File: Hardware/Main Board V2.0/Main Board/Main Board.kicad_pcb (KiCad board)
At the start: 2 copper layers, 61 parts, among them J1 Module A1, J2 Module A2, J3 Module A3, J4 Module B1, J5 Module B2, J6 Module B3, U1 74AHCT595, U2 74AHCT595, U3 74AHCT595, U4 74AHCT595, U5 ESP32-WROOM-32UE-H4, U6 ESP32-WROOM-32UE-H4, U7 CP2104, U8 CP2104, U9 GT-USB-7051A

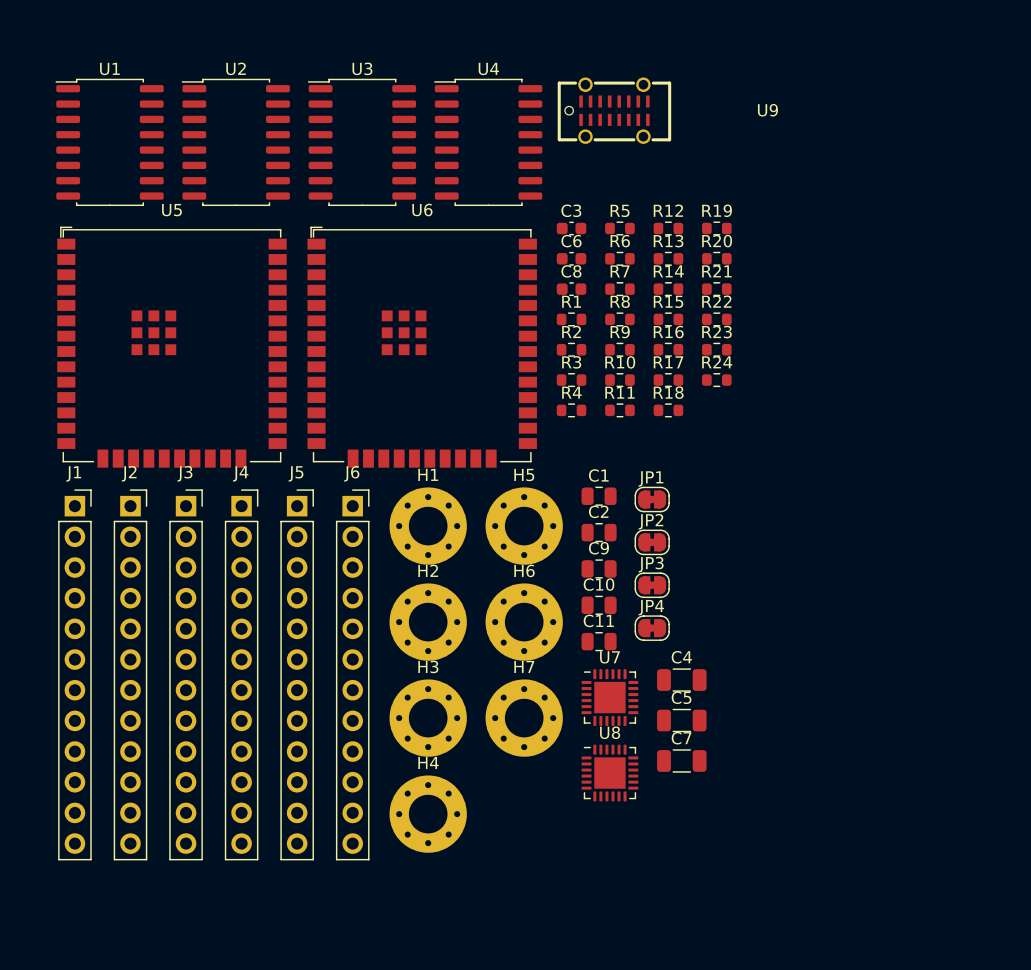
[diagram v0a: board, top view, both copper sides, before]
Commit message: Work on shift registers, and power for esp32
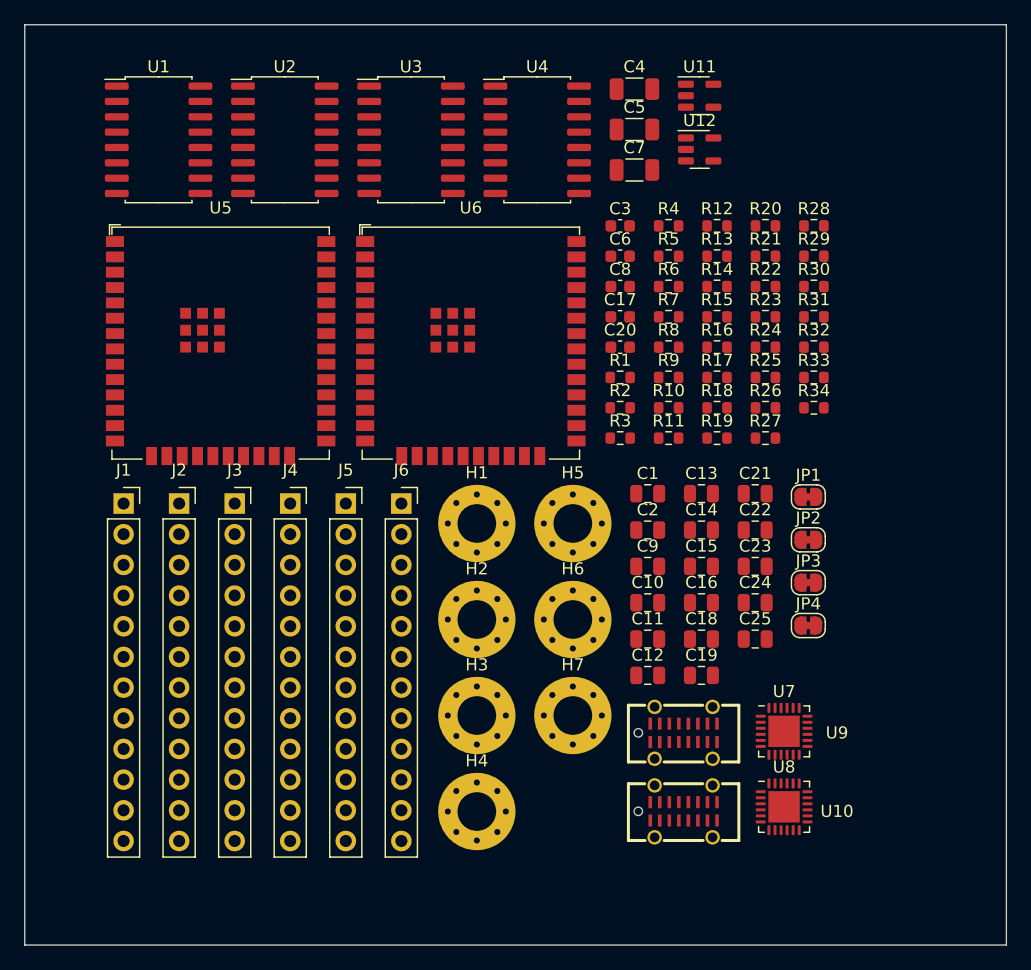
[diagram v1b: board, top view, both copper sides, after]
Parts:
- added C12: 1uF, Capacitor_SMD:C_0805_2012Metric, F.Cu at (71.9, 69.1)
- added C13: 1uF, Capacitor_SMD:C_0805_2012Metric, F.Cu at (76.4, 54.1)
- added C14: 10uF, Capacitor_SMD:C_0805_2012Metric, F.Cu at (76.4, 57.1)
- added C15: 4.7uF, Capacitor_SMD:C_0805_2012Metric, F.Cu at (76.4, 60.1)
- added C16: 1uF, Capacitor_SMD:C_0805_2012Metric, F.Cu at (76.4, 63.1)
- added C17: 100nF, Capacitor_SMD:C_0603_1608Metric, F.Cu at (69.6, 39.4)
- added C18: 4.7uF, Capacitor_SMD:C_0805_2012Metric, F.Cu at (76.4, 66.1)
- added C19: 1uF, Capacitor_SMD:C_0805_2012Metric, F.Cu at (76.4, 69.1)
- added C20: 100nF, Capacitor_SMD:C_0603_1608Metric, F.Cu at (69.6, 41.9)
- added C21: 10uF, Capacitor_SMD:C_0805_2012Metric, F.Cu at (80.8, 54.1)
- added C22: 1uF, Capacitor_SMD:C_0805_2012Metric, F.Cu at (80.8, 57.1)
- added C23: 10uF, Capacitor_SMD:C_0805_2012Metric, F.Cu at (80.8, 60.1)
- added C24: 10uF, Capacitor_SMD:C_0805_2012Metric, F.Cu at (80.8, 63.1)
- added C25: 1uF, Capacitor_SMD:C_0805_2012Metric, F.Cu at (80.8, 66.1)
- added R25: 5.1K, Resistor_SMD:R_0603_1608Metric, F.Cu at (81.7, 44.4)
- added R26: 5.1K, Resistor_SMD:R_0603_1608Metric, F.Cu at (81.7, 47.0)
- added R27: 5.1K, Resistor_SMD:R_0603_1608Metric, F.Cu at (81.7, 49.5)
- added R28: 5.1K, Resistor_SMD:R_0603_1608Metric, F.Cu at (85.7, 31.9)
- added R29: 10K, Resistor_SMD:R_0603_1608Metric, F.Cu at (85.7, 34.4)
- added R30: 10K, Resistor_SMD:R_0603_1608Metric, F.Cu at (85.7, 36.9)
- added R31: 100K, Resistor_SMD:R_0603_1608Metric, F.Cu at (85.7, 39.4)
- added R32: 4.3K, Resistor_SMD:R_0603_1608Metric, F.Cu at (85.7, 41.9)
- added R33: 100K, Resistor_SMD:R_0603_1608Metric, F.Cu at (85.7, 44.4)
- added R34: 4.3K, Resistor_SMD:R_0603_1608Metric, F.Cu at (85.7, 47.0)
- added U10: GT-USB-7051A, KiCad:GT-USB-7051A, F.Cu at (74.9, 80.4)
- added U11: AP2112K-3.3, Package_TO_SOT_SMD:SOT-23-5, F.Cu at (76.2, 21.1)
- added U12: AP2112K-3.3, Package_TO_SOT_SMD:SOT-23-5, F.Cu at (76.2, 25.6)
- moved U9 51.8 mm to (74.9, 73.9)
- moved C4 49.1 mm to (70.8, 20.6)
- moved C7 49.1 mm to (70.8, 27.3)
- moved C5 49.1 mm to (70.8, 23.9)
- moved R19 17.4 mm to (77.6, 49.5)
- moved R4 17.3 mm to (73.6, 31.9)
- moved U7 14.7 mm to (83.2, 73.7)
- moved U8 14.7 mm to (83.2, 80.0)
- moved JP1 12.9 mm to (85.2, 54.3)
- moved JP2 12.9 mm to (85.2, 57.9)
- moved JP3 12.9 mm to (85.2, 61.4)
- moved JP4 12.9 mm to (85.2, 65.0)
- moved R3 6.27 mm to (69.6, 49.5)
- moved R1 6.27 mm to (69.6, 44.4)
- moved R2 6.27 mm to (69.6, 47.0)
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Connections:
- C10 pad 1: unconnected-(C10-Pad1) -> Net-(U7-VPP)
- C10 pad 2: unconnected-(C10-Pad2) -> GND
- C11 pad 1: unconnected-(C11-Pad1) -> GND
- C11 pad 2: unconnected-(C11-Pad2) -> Net-(U8-VPP)
- C5 pad 1: +3V3 -> A_VCC
- C6 pad 1: +3V3 -> A_VCC
- C7 pad 1: +3V3 -> B_VCC
- C8 pad 1: +3V3 -> B_VCC
- J1 pad 3: VCC -> A_VCC
- J2 pad 3: VCC -> A_VCC
- J3 pad 3: VCC -> A_VCC
- J4 pad 3: VCC -> B_VCC
- J5 pad 3: VCC -> B_VCC
- J6 pad 3: VCC -> B_VCC
- R23 pad 2: +3V3 -> A_VCC
- R24 pad 2: +3V3 -> B_VCC
- U5 pad 2: +3V3 -> B_VCC
- U6 pad 2: +3V3 -> A_VCC
- U7 pad 16: unconnected-(U7-VPP-Pad16) -> Net-(U7-VPP)
- U7 pad 3: Net-(D19-L3) -> A_D+
- U7 pad 4: Net-(D19-L2) -> A_D-
- U7 pad 5: +3V3 -> A_VCC
- U7 pad 6: +3V3 -> A_VCC
- U7 pad 7: +3V3 -> A_VCC
- U8 pad 16: unconnected-(U8-VPP-Pad16) -> Net-(U8-VPP)
- U8 pad 3: Net-(D20-L3) -> B_D+
- U8 pad 4: Net-(D20-L2) -> B_D-
- U8 pad 5: +3V3 -> B_VCC
- U8 pad 6: +3V3 -> B_VCC
- U8 pad 7: +3V3 -> B_VCC
- U9 pad A1: unconnected-(U9-GND-PadA1) -> GND
- U9 pad A12: unconnected-(U9-GND-PadA12) -> GND
- U9 pad A4: unconnected-(U9-VBUS-PadA4) -> Net-(D22-A)
- U9 pad A5: unconnected-(U9-CC1-PadA5) -> B_CC1
- U9 pad A6: unconnected-(U9-DP1-PadA6) -> B_D+
- U9 pad A7: unconnected-(U9-DN1-PadA7) -> B_D-
- U9 pad A9: unconnected-(U9-VBUS-PadA9) -> Net-(D22-A)
- U9 pad B1: unconnected-(U9-GND-PadB1) -> GND
- U9 pad B12: unconnected-(U9-GND-PadB12) -> GND
- U9 pad B4: unconnected-(U9-VBUS-PadB4) -> Net-(D22-A)
- U9 pad B5: unconnected-(U9-CC2-PadB5) -> B_CC2
- U9 pad B6: unconnected-(U9-DP2-PadB6) -> B_D+
- U9 pad B7: unconnected-(U9-DN2-PadB7) -> B_D-
- U9 pad B9: unconnected-(U9-VBUS-PadB9) -> Net-(D22-A)
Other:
- board outline added: 81.3 x 76.2 mm

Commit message: v2 work
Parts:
- removed C22, C25: 1uF, Capacitor_SMD:C_0805_2012Metric
- removed C24: 10uF, Capacitor_SMD:C_0805_2012Metric
- removed J2: Module A2, Connector_PinSocket_2.54mm:PinSocket_1x12_P2.54mm_Vertical
- removed J3: Module A3, Connector_PinSocket_2.54mm:PinSocket_1x12_P2.54mm_Vertical
- removed J4: Module B1, Connector_PinSocket_2.54mm:PinSocket_1x12_P2.54mm_Vertical
- removed J6: Module B3, Connector_PinSocket_2.54mm:PinSocket_1x12_P2.54mm_Vertical
- added C26: 100nF, Capacitor_SMD:C_0603_1608Metric, F.Cu at (84.1, 121.3)
- added C27: 1uF, Capacitor_SMD:C_0805_2012Metric, F.Cu at (30.0, 178.4)
- added C28: 22uF, Capacitor_SMD:C_1206_3216Metric, F.Cu at (117.0, 119.0)
- added C29: 100nF, Capacitor_SMD:C_0603_1608Metric, F.Cu at (84.1, 123.8)
- added C30: 4.7uF, Capacitor_SMD:C_0805_2012Metric, F.Cu at (30.0, 181.4)
- added C31: 1uF, Capacitor_SMD:C_0805_2012Metric, F.Cu at (34.5, 169.4)
- added C32: 100nF, Capacitor_SMD:C_0603_1608Metric, F.Cu at (84.1, 126.3)
- added C33: 4.7uF, Capacitor_SMD:C_0805_2012Metric, F.Cu at (34.5, 172.4)
- added C34: 22uF, Capacitor_SMD:C_1206_3216Metric, F.Cu at (117.0, 122.3)
- added C35: 10uF, Capacitor_SMD:C_0805_2012Metric, F.Cu at (34.5, 175.4)
- added C36: 4.7uF, Capacitor_SMD:C_0805_2012Metric, F.Cu at (34.5, 178.4)
- added C37: 1uF, Capacitor_SMD:C_0805_2012Metric, F.Cu at (34.5, 181.4)
- added C38: 100nF, Capacitor_SMD:C_0603_1608Metric, F.Cu at (84.1, 128.8)
- added C39: 10nF, Capacitor_SMD:C_0603_1608Metric, F.Cu at (84.1, 131.3)
- added D1: Emerald, LED_SMD:LED_0603_1608Metric, F.Cu at (96.7, 80.4)
- added D10: Emerald, LED_SMD:LED_0603_1608Metric, F.Cu at (100.8, 88.2)
- added D11: Emerald, LED_SMD:LED_0603_1608Metric, F.Cu at (100.8, 90.8)
- added D12: Emerald, LED_SMD:LED_0603_1608Metric, F.Cu at (100.8, 93.4)
- added D13: Emerald, LED_SMD:LED_0603_1608Metric, F.Cu at (104.8, 80.4)
- added D14: Emerald, LED_SMD:LED_0603_1608Metric, F.Cu at (104.8, 83.0)
- added D15: Emerald, LED_SMD:LED_0603_1608Metric, F.Cu at (104.8, 85.6)
- added D16: Emerald, LED_SMD:LED_0603_1608Metric, F.Cu at (104.8, 88.2)
- added D17: Emerald, LED_SMD:LED_0603_1608Metric, F.Cu at (104.8, 90.8)
- added D18: Emerald, LED_SMD:LED_0603_1608Metric, F.Cu at (104.8, 93.4)
- added D2: Emerald, LED_SMD:LED_0603_1608Metric, F.Cu at (96.7, 83.0)
- added D22: Emerald, LED_SMD:LED_0603_1608Metric, F.Cu at (108.9, 80.4)
- added D23: Emerald, LED_SMD:LED_0603_1608Metric, F.Cu at (108.9, 83.0)
- added D24: SS54, Diode_SMD:D_SMA, F.Cu at (119.3, 99.8)
- added D25: Emerald, LED_SMD:LED_0603_1608Metric, F.Cu at (108.9, 85.6)
- added D26: Emerald, LED_SMD:LED_0603_1608Metric, F.Cu at (108.9, 88.2)
- added D3: Emerald, LED_SMD:LED_0603_1608Metric, F.Cu at (96.7, 85.6)
- added D4: Emerald, LED_SMD:LED_0603_1608Metric, F.Cu at (96.7, 88.2)
- added D5: Emerald, LED_SMD:LED_0603_1608Metric, F.Cu at (96.7, 90.8)
- added D6: Emerald, LED_SMD:LED_0603_1608Metric, F.Cu at (96.7, 93.4)
- added D7: Emerald, LED_SMD:LED_0603_1608Metric, F.Cu at (100.8, 80.4)
- added D8: Emerald, LED_SMD:LED_0603_1608Metric, F.Cu at (100.8, 83.0)
- added D9: Emerald, LED_SMD:LED_0603_1608Metric, F.Cu at (100.8, 85.6)
- added H10: MountingHole, MountingHole:MountingHole_3.2mm_M3_Pad_Via, F.Cu at (-140.0, -16.0)
- added H11: MountingHole, MountingHole:MountingHole_3.2mm_M3_Pad_Via, F.Cu at (-48.0, 76.0)
- added H8: MountingHole, MountingHole:MountingHole_3.2mm_M3_Pad_Via, F.Cu at (-140.0, 76.0)
- added H9: MountingHole, MountingHole:MountingHole_3.2mm_M3_Pad_Via, F.Cu at (-48.3, -15.7)
- added J26: Conn_02x03_Top_Bottom, KiCad:DB2ERH-2.5-2-3P-GN, F.Cu at (-120.0, 60.0)
- added J27: Conn_02x03_Top_Bottom, KiCad:DB2ERH-2.5-2-3P-GN, F.Cu at (-110.0, 60.0)
- added J28: Conn_02x03_Top_Bottom, KiCad:DB2ERH-2.5-2-3P-GN, F.Cu at (-100.0, 60.0)
- added J29: Conn_02x03_Top_Bottom, KiCad:DB2ERH-2.5-2-3P-GN, F.Cu at (-90.0, 60.0)
- added J30: Conn_02x03_Top_Bottom, KiCad:DB2ERH-2.5-2-3P-GN, F.Cu at (-80.0, 60.0)
- added J39: Conn_02x03_Top_Bottom, KiCad:DB2ERH-2.5-2-3P-GN, F.Cu at (-70.0, 60.0)
- added J40: Conn_02x08_Top_Bottom, KiCad:DB2ERH-2.5-2-8P-GN, F.Cu at (-80.0, -15.0)
- added J8: Conn_02x08_Top_Bottom, KiCad:DB2ERH-2.5-2-8P-GN, F.Cu at (-102.5, -15.0)
- added K1: G2RL-1-E-DC12, Relay_THT:Relay_SPDT_Schrack-RT1-16A-FormC_RM5mm, F.Cu at (-77.2, 41.2)
- added K2: G2RL-1-E-DC12, Relay_THT:Relay_SPDT_Schrack-RT1-16A-FormC_RM5mm, F.Cu at (-35.3, 22.5)
- added L3: 15uH, Inductor_SMD:L_Sunlord_MWSA0603S, F.Cu at (119.1, 128.1)
- added Q1: BSS138, Package_TO_SOT_SMD:SOT-23, F.Cu at (40.3, 159.7)
- added Q10: BSS138, Package_TO_SOT_SMD:SOT-23, F.Cu at (45.2, 173.1)
- added Q11: BSS138, Package_TO_SOT_SMD:SOT-23, F.Cu at (45.2, 177.5)
- added Q12: BSS138, Package_TO_SOT_SMD:SOT-23, F.Cu at (45.2, 182.0)
- added Q13: BSS138, Package_TO_SOT_SMD:SOT-23, F.Cu at (50.1, 159.7)
- added Q14: BSS138, Package_TO_SOT_SMD:SOT-23, F.Cu at (50.1, 164.2)
- added Q15: BSS138, Package_TO_SOT_SMD:SOT-23, F.Cu at (50.1, 168.6)
- added Q16: BSS138, Package_TO_SOT_SMD:SOT-23, F.Cu at (50.1, 173.1)
- added Q17: BSS138, Package_TO_SOT_SMD:SOT-23, F.Cu at (50.1, 177.5)
- added Q18: BSS138, Package_TO_SOT_SMD:SOT-23, F.Cu at (50.1, 182.0)
- added Q2: BSS138, Package_TO_SOT_SMD:SOT-23, F.Cu at (40.3, 164.2)
- added Q3: BSS138, Package_TO_SOT_SMD:SOT-23, F.Cu at (40.3, 168.6)
- added Q4: BSS138, Package_TO_SOT_SMD:SOT-23, F.Cu at (40.3, 173.1)
- added Q5: BSS138, Package_TO_SOT_SMD:SOT-23, F.Cu at (40.3, 177.5)
- added Q6: BSS138, Package_TO_SOT_SMD:SOT-23, F.Cu at (40.3, 182.0)
- added Q7: BSS138, Package_TO_SOT_SMD:SOT-23, F.Cu at (45.2, 159.7)
- added Q8: BSS138, Package_TO_SOT_SMD:SOT-23, F.Cu at (45.2, 164.2)
- added Q9: BSS138, Package_TO_SOT_SMD:SOT-23, F.Cu at (45.2, 168.6)
- added R100: 2K, Resistor_SMD:R_0603_1608Metric_Pad0.98x0.95mm_HandSolder, F.Cu at (59.0, 166.3)
- added R101: 2K, Resistor_SMD:R_0603_1608Metric_Pad0.98x0.95mm_HandSolder, F.Cu at (63.4, 158.8)
- added R102: 2K, Resistor_SMD:R_0603_1608Metric_Pad0.98x0.95mm_HandSolder, F.Cu at (63.4, 161.3)
- added R103: 2K, Resistor_SMD:R_0603_1608Metric_Pad0.98x0.95mm_HandSolder, F.Cu at (63.4, 163.8)
- added R104: 2K, Resistor_SMD:R_0603_1608Metric_Pad0.98x0.95mm_HandSolder, F.Cu at (63.4, 166.3)
- added R105: 510R, Resistor_SMD:R_0603_1608Metric, F.Cu at (112.1, 111.3)
- added R106: 510R, Resistor_SMD:R_0603_1608Metric, F.Cu at (112.1, 113.8)
- added R107: 510R, Resistor_SMD:R_0603_1608Metric, F.Cu at (112.1, 116.3)
- added R108: 510R, Resistor_SMD:R_0603_1608Metric, F.Cu at (112.1, 118.8)
- added R109: 510R, Resistor_SMD:R_0603_1608Metric, F.Cu at (112.1, 121.3)
- added R110: 510R, Resistor_SMD:R_0603_1608Metric, F.Cu at (112.1, 123.8)
- added R111: 510R, Resistor_SMD:R_0603_1608Metric, F.Cu at (112.1, 126.3)
- added R112: 510R, Resistor_SMD:R_0603_1608Metric, F.Cu at (112.1, 128.8)
- added R113: 510R, Resistor_SMD:R_0603_1608Metric, F.Cu at (112.1, 131.3)
- added R35: 200R, Resistor_SMD:R_0603_1608Metric, F.Cu at (96.1, 113.8)
- added R36: 200R, Resistor_SMD:R_0603_1608Metric, F.Cu at (96.1, 116.3)
- added R37: 200R, Resistor_SMD:R_0603_1608Metric, F.Cu at (96.1, 118.8)
- added R38: 1K, Resistor_SMD:R_0603_1608Metric, F.Cu at (96.1, 121.3)
- added R39: 1K, Resistor_SMD:R_0603_1608Metric, F.Cu at (96.1, 123.8)
- added R40: 1K, Resistor_SMD:R_0603_1608Metric, F.Cu at (96.1, 126.3)
- added R41: 1K, Resistor_SMD:R_0603_1608Metric, F.Cu at (96.1, 128.8)
- added R42: 1K, Resistor_SMD:R_0603_1608Metric, F.Cu at (96.1, 131.3)
- added R43: 1K, Resistor_SMD:R_0603_1608Metric, F.Cu at (96.1, 133.9)
- added R44: 1K, Resistor_SMD:R_0603_1608Metric, F.Cu at (96.1, 136.4)
- added R45: 1K, Resistor_SMD:R_0603_1608Metric, F.Cu at (100.1, 103.7)
- added R46: 1K, Resistor_SMD:R_0603_1608Metric, F.Cu at (100.1, 106.2)
- added R47: 10K, Resistor_SMD:R_0603_1608Metric, F.Cu at (100.1, 108.8)
- added R48: 10K, Resistor_SMD:R_0603_1608Metric, F.Cu at (100.1, 111.3)
- added R49: 10K, Resistor_SMD:R_0603_1608Metric, F.Cu at (100.1, 113.8)
- added R50: 10K, Resistor_SMD:R_0603_1608Metric, F.Cu at (100.1, 116.3)
- added R51: 10K, Resistor_SMD:R_0603_1608Metric, F.Cu at (100.1, 118.8)
- added R52: 10K, Resistor_SMD:R_0603_1608Metric, F.Cu at (100.1, 121.3)
- added R53: 10K, Resistor_SMD:R_0603_1608Metric, F.Cu at (100.1, 123.8)
- added R54: 10K, Resistor_SMD:R_0603_1608Metric, F.Cu at (100.1, 126.3)
- added R55: 10K, Resistor_SMD:R_0603_1608Metric, F.Cu at (100.1, 128.8)
- added R56: 510R, Resistor_SMD:R_0603_1608Metric, F.Cu at (100.1, 131.3)
- added R57: 510R, Resistor_SMD:R_0603_1608Metric, F.Cu at (100.1, 133.9)
- added R58: 510R, Resistor_SMD:R_0603_1608Metric, F.Cu at (100.1, 136.4)
- added R59: 510R, Resistor_SMD:R_0603_1608Metric, F.Cu at (104.1, 103.7)
- added R60: 510R, Resistor_SMD:R_0603_1608Metric, F.Cu at (104.1, 106.2)
- added R61: 510R, Resistor_SMD:R_0603_1608Metric, F.Cu at (104.1, 108.8)
- added R62: 510R, Resistor_SMD:R_0603_1608Metric, F.Cu at (104.1, 111.3)
- added R63: 510R, Resistor_SMD:R_0603_1608Metric, F.Cu at (104.1, 113.8)
- added R64: 510R, Resistor_SMD:R_0603_1608Metric, F.Cu at (104.1, 116.3)
- added R65: 510R, Resistor_SMD:R_0603_1608Metric, F.Cu at (104.1, 118.8)
- added R66: 510R, Resistor_SMD:R_0603_1608Metric, F.Cu at (104.1, 121.3)
- added R67: 510R, Resistor_SMD:R_0603_1608Metric, F.Cu at (104.1, 123.8)
- added R68: 510R, Resistor_SMD:R_0603_1608Metric, F.Cu at (104.1, 126.3)
- added R69: 510R, Resistor_SMD:R_0603_1608Metric, F.Cu at (104.1, 128.8)
- added R70: 510R, Resistor_SMD:R_0603_1608Metric, F.Cu at (104.1, 131.3)
- added R74: 5.1K, Resistor_SMD:R_0603_1608Metric, F.Cu at (104.1, 133.9)
- added R75: 5.1K, Resistor_SMD:R_0603_1608Metric, F.Cu at (104.1, 136.4)
- added R76: 100K, Resistor_SMD:R_0603_1608Metric, F.Cu at (108.1, 103.7)
- added R77: 4.7K, Resistor_SMD:R_0603_1608Metric, F.Cu at (108.1, 106.2)
- added R78: 4.3K, Resistor_SMD:R_0603_1608Metric, F.Cu at (108.1, 108.8)
- added R79: 1K, Resistor_SMD:R_0603_1608Metric, F.Cu at (108.1, 111.3)
- added R80: 10K, Resistor_SMD:R_0603_1608Metric, F.Cu at (108.1, 113.8)
- added R81: 10K, Resistor_SMD:R_0603_1608Metric, F.Cu at (108.1, 116.3)
- added R83: 10K, Resistor_SMD:R_0603_1608Metric, F.Cu at (108.1, 121.3)
- added R84: 3.24K, Resistor_SMD:R_0603_1608Metric, F.Cu at (108.1, 123.8)
- added R85: 430R, Resistor_SMD:R_0603_1608Metric, F.Cu at (108.1, 126.3)
- added R87: 10K, Resistor_SMD:R_0603_1608Metric, F.Cu at (108.1, 131.3)
- added R88: 5.1K, Resistor_SMD:R_0603_1608Metric, F.Cu at (108.1, 133.9)
- added R89: 5.1K, Resistor_SMD:R_0603_1608Metric, F.Cu at (108.1, 136.4)
- added R90: 4.7K, Resistor_SMD:R_0603_1608Metric, F.Cu at (112.1, 103.7)
- added R91: 10K, Resistor_SMD:R_0603_1608Metric, F.Cu at (112.1, 106.2)
- added R92: 10K, Resistor_SMD:R_0603_1608Metric, F.Cu at (112.1, 108.8)
- added R93: 2K, Resistor_SMD:R_0603_1608Metric_Pad0.98x0.95mm_HandSolder, F.Cu at (54.7, 158.8)
- added R94: 2K, Resistor_SMD:R_0603_1608Metric_Pad0.98x0.95mm_HandSolder, F.Cu at (54.7, 161.3)
- added R95: 2K, Resistor_SMD:R_0603_1608Metric_Pad0.98x0.95mm_HandSolder, F.Cu at (54.7, 163.8)
- added R96: 2K, Resistor_SMD:R_0603_1608Metric_Pad0.98x0.95mm_HandSolder, F.Cu at (54.7, 166.3)
- added R97: 2K, Resistor_SMD:R_0603_1608Metric_Pad0.98x0.95mm_HandSolder, F.Cu at (59.0, 158.8)
- added R98: 2K, Resistor_SMD:R_0603_1608Metric_Pad0.98x0.95mm_HandSolder, F.Cu at (59.0, 161.3)
- added R99: 2K, Resistor_SMD:R_0603_1608Metric_Pad0.98x0.95mm_HandSolder, F.Cu at (59.0, 163.8)
- added U13: Module A1, Connector_PinSocket_2.54mm:PinSocket_1x12_P2.54mm_Vertical, F.Cu at (69.7, 140.4)
- added U14: Module B1, Connector_PinSocket_2.54mm:PinSocket_1x12_P2.54mm_Vertical, F.Cu at (74.3, 140.4)
- added U16: Module A2, Connector_PinSocket_2.54mm:PinSocket_1x12_P2.54mm_Vertical, F.Cu at (78.9, 140.4)
- added U17: Module B2, Connector_PinSocket_2.54mm:PinSocket_1x12_P2.54mm_Vertical, F.Cu at (83.5, 140.4)
- added U18: GT-USB-7051A, KiCad:GT-USB-7051A, F.Cu at (-99.6, 34.8)
- added U19: Module A3, Connector_PinSocket_2.54mm:PinSocket_1x12_P2.54mm_Vertical, F.Cu at (88.1, 140.4)
- added U20: Module B3, Connector_PinSocket_2.54mm:PinSocket_1x12_P2.54mm_Vertical, F.Cu at (92.7, 140.4)
- added U21: CP2104, Package_DFN_QFN:QFN-24-1EP_4x4mm_P0.5mm_EP2.6x2.6mm, F.Cu at (118.4, 88.5)
- added U22: Module A4, Connector_PinSocket_2.54mm:PinSocket_1x12_P2.54mm_Vertical, F.Cu at (97.3, 140.4)
- added U23: ESP32_38p, KiCad:MH ET LIVE ESP-32 Dev Kit, F.Cu at (52.6, 127.9)
- added U24: ELQ3H7, KiCad:ELQ3H7 SOP-16_4.4x10.4mm_P1.27mm, F.Cu at (69.4, 172.4)
- added U25: ELQ3H7, KiCad:ELQ3H7 SOP-16_4.4x10.4mm_P1.27mm, F.Cu at (79.2, 172.4)
- added U26: ELQ3H7, KiCad:ELQ3H7 SOP-16_4.4x10.4mm_P1.27mm, F.Cu at (89.1, 172.4)
- added U27: ULN2003A, Package_SO:SOIC-16_3.9x9.9mm_P1.27mm, F.Cu at (121.5, 175.6)
- added U28: ULN2003A, Package_SO:SOIC-16_3.9x9.9mm_P1.27mm, F.Cu at (363.1, 151.8)
- C1: value 10uF -> 1uF
- C10, C15: value 4.7uF -> 10uF
- C11, C18: value 4.7uF -> 1uF
- C12: value 1uF -> 10uF
- C13: value 1uF -> 100nF; footprint Capacitor_SMD:C_0805_2012Metric -> Capacitor_SMD:C_0603_1608Metric
- C16: value 1uF -> 4.7uF
- C17: value 100nF -> 10uF; footprint Capacitor_SMD:C_0603_1608Metric -> Capacitor_SMD:C_0805_2012Metric
- C19: value 1uF -> 120uF; footprint Capacitor_SMD:C_0805_2012Metric -> Capacitor_SMD:CP_Elec_10x12.6
- C2: value 1uF -> 22uF; footprint Capacitor_SMD:C_0805_2012Metric -> Capacitor_SMD:C_1206_3216Metric
- C20, C8: value 100nF -> 120uF; footprint Capacitor_SMD:C_0603_1608Metric -> Capacitor_SMD:CP_Elec_10x12.6
- C21: value 10uF -> 10nF; footprint Capacitor_SMD:C_0805_2012Metric -> Capacitor_SMD:C_0603_1608Metric
- C23: value 10uF -> 330uF; footprint Capacitor_SMD:C_0805_2012Metric -> Capacitor_Tantalum_SMD:CP_EIA-7343-31_Kemet-D
- C4, C5, C7: value 22uF -> 100nF; footprint Capacitor_SMD:C_1206_3216Metric -> Capacitor_SMD:C_0603_1608Metric
- J1: value Module A1 -> Micro_SD_Card; footprint Connector_PinSocket_2.54mm:PinSocket_1x12_P2.54mm_Vertical -> Connector_Card:microSD_HC_Hirose_DM3AT-SF-PEJM5
- J5: value Module B2 -> Conn_02x08_Top_Bottom; footprint Connector_PinSocket_2.54mm:PinSocket_1x12_P2.54mm_Vertical -> KiCad:DB2ERH-2.5-2-8P-GN
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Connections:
- net B_GPIO_1 renamed GPIO_1
- net B_GPIO_16 renamed GPIO_16
- net B_GPIO_18 renamed GPIO_18
- net B_GPIO_19 renamed GPIO_19
- net B_GPIO_2 renamed GPIO_2
- net B_GPIO_23 renamed GPIO_23
- net B_GPIO_25 renamed GPIO_25
- net B_GPIO_26 renamed GPIO_26
- net B_GPIO_27 renamed GPIO_27
- net B_GPIO_3 renamed GPIO_3
- net B_GPIO_32 renamed GPIO_32
- net B_GPIO_33 renamed GPIO_33
- net B_GPIO_36 renamed GPIO_36
- net B_GPIO_39 renamed GPIO_39
- net B_GPIO_4 renamed GPIO_4
- net B_GPIO_5 renamed GPIO_5
- C1 pad 1: unconnected-(C1-Pad1) -> +12V
- C1 pad 2: unconnected-(C1-Pad2) -> RESET
- C10 pad 1: Net-(U7-VPP) -> +12V
- C10 pad 2: GND -> +12V
- C11 pad 1: GND -> +3V3
- C11 pad 2: Net-(U8-VPP) -> +12V
- C12 pad 1: GND -> +24V
- C12 pad 2: A_RESET -> +12V
- C13 pad 1: GND -> +3V3
- C13 pad 2: B_RESET -> +12V
- C14 pad 1: Net-(U11-VIN) -> +24V
- C14 pad 2: GND -> +12V
- C15 pad 1: A_VCC -> +3V3
- C15 pad 2: GND -> +12V
- C16 pad 1: A_VCC -> Net-(U9-VPP)
- C16 pad 2: GND -> +12V
- C17 pad 1: A_VCC -> +24V
- C17 pad 2: GND -> +12V
- C18 pad 1: B_VCC -> +3V3
- C18 pad 2: GND -> +12V
- C19 pad 1: B_VCC -> Net-(U7-FB)
- C19 pad 2: GND -> +12V
- C2 pad 1: unconnected-(C2-Pad1) -> +3V3
- C2 pad 2: unconnected-(C2-Pad2) -> +12V
- C20 pad 1: B_VCC -> +12V
- C20 pad 2: GND -> +12V
- C21 pad 1: A_VCC -> Net-(U10-BOOT)
- C21 pad 2: GND -> Net-(D24-K)
- C23 pad 1: Net-(U12-VIN) -> +12V
- C23 pad 2: GND -> +12V
- C3 pad 1: unconnected-(C3-Pad1) -> +3V3
- C3 pad 2: unconnected-(C3-Pad2) -> +12V
- C4 pad 1: unconnected-(C4-Pad1) -> +3V3
- C4 pad 2: unconnected-(C4-Pad2) -> +12V
- C5 pad 1: A_VCC -> +3V3
- C5 pad 2: GND -> +12V
- C6 pad 1: A_VCC -> +3V3
- C6 pad 2: GND -> +12V
- C7 pad 1: B_VCC -> +3V3
- C7 pad 2: GND -> +12V
- C8 pad 1: B_VCC -> +24V
- C8 pad 2: GND -> +12V
- C9 pad 1: unconnected-(C9-Pad1) -> +3V3
- C9 pad 2: unconnected-(C9-Pad2) -> +12V
- H1 pad 1: GND -> +12V
- H2 pad 1: GND -> +12V
- H3 pad 1: GND -> +12V
- H4 pad 1: GND -> +12V
- H5 pad 1: GND -> +12V
- H6 pad 1: GND -> +12V
- H7 pad 1: GND -> +12V
- J1 pad 1: GND -> unconnected-(J1-DAT2-Pad1)
- J1 pad 10: A_CS -> (no net)
- J1 pad 11: A_MISO -> (no net)
- J1 pad 2: Vdrive -> CS_SD
- J1 pad 3: A_VCC -> MOSI
- J1 pad 4: unconnected-(J1-1-Pad4) -> +3V3
- J1 pad 5: unconnected-(J1-2-Pad5) -> SCLK
- J1 pad 6: unconnected-(J1-3-Pad6) -> +12V
- J1 pad 7: unconnected-(J1-4-Pad7) -> MISO
- J1 pad 8: A_SCLK -> unconnected-(J1-DAT1-Pad8)
- J1 pad 9: A_MOSI -> +12V
- J5 pad 1: GND -> Y_Enable_HV
- J5 pad 10: B_CS -> Net-(J5-Pin_10)
- J5 pad 11: B_MISO -> B_Step_HV
- J5 pad 12: GND -> Net-(J5-Pin_12)
- J5 pad 2: Vdrive -> Net-(J5-Pin_2)
- J5 pad 3: B_VCC -> Y_Step_HV
- J5 pad 4: unconnected-(J5-1-Pad4) -> Net-(J5-Pin_4)
- J5 pad 5: unconnected-(J5-2-Pad5) -> Y_Dir_HV
- J5 pad 6: unconnected-(J5-3-Pad6) -> Net-(J5-Pin_6)
- J5 pad 8: B_SCLK -> Net-(J5-Pin_8)
- J5 pad 9: B_MOSI -> B_Enable_HV
- JP1 pad 2: A_GPIO_0 -> GPIO_0
- JP2 pad 2: A_RESET -> RESET
- R1 pad 1: B_RTS -> Net-(Q1-G)
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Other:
- board size 81.3 x 76.2 mm -> 100 x 100 mm

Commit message: start a teensy version with migration to grblHAL for built in THC
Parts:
- removed C31: 1uF, Capacitor_SMD:C_0805_2012Metric
- removed C32: 100nF, Capacitor_SMD:C_0603_1608Metric
- removed C33: 4.7uF, Capacitor_SMD:C_0805_2012Metric
- removed H10, H11, H8, H9: MountingHole, MountingHole:MountingHole_3.2mm_M3_Pad_Via
- removed JP3, JP4: SolderJumper_2_Bridged, Jumper:SolderJumper-2_P1.3mm_Bridged_RoundedPad1.0x1.5mm
- removed Q1, Q10, Q11, Q12, Q13, Q14, Q15, Q16, Q17, Q18, Q2, Q3, Q4, Q5, Q6, Q7, Q8, Q9: BSS138, Package_TO_SOT_SMD:SOT-23
- removed U18: GT-USB-7051A, KiCad:GT-USB-7051A
- removed U20: Module B3, Connector_PinSocket_2.54mm:PinSocket_1x12_P2.54mm_Vertical
- removed U21: CP2104, Package_DFN_QFN:QFN-24-1EP_4x4mm_P0.5mm_EP2.6x2.6mm
- added C22: 100nF, Capacitor_SMD:C_0603_1608Metric, F.Cu at (208.6, 72.1)
- added C24: 100nF, Capacitor_SMD:C_0603_1608Metric, F.Cu at (208.6, 74.6)
- added C25: 100nF, Capacitor_SMD:C_0603_1608Metric, F.Cu at (208.6, 77.1)
- added C40: 100nF, Capacitor_SMD:C_0603_1608Metric, F.Cu at (208.6, 79.7)
- added D27: MSCD104H, Diode_SMD:D_0805_2012Metric_Pad1.15x1.40mm_HandSolder, F.Cu at (216.0, 90.0)
- added D28: MSCD104H, Diode_SMD:D_0805_2012Metric_Pad1.15x1.40mm_HandSolder, F.Cu at (216.0, 93.0)
- added D31: Emerald, LED_SMD:LED_0603_1608Metric, F.Cu at (224.7, 72.2)
- added D32: Emerald, LED_SMD:LED_0603_1608Metric, F.Cu at (224.7, 74.8)
- added D33: Emerald, LED_SMD:LED_0603_1608Metric, F.Cu at (224.7, 77.3)
- added D34: Emerald, LED_SMD:LED_0603_1608Metric, F.Cu at (224.7, 79.9)
- added D35: Emerald, LED_SMD:LED_0603_1608Metric, F.Cu at (224.7, 82.5)
- added FB1: BLM18HE152SN1D, Resistor_SMD:R_0603_1608Metric_Pad0.98x0.95mm_HandSolder, F.Cu at (228.9, 72.1)
- added FB2: BLM18HE152SN1D, Resistor_SMD:R_0603_1608Metric_Pad0.98x0.95mm_HandSolder, F.Cu at (228.9, 74.6)
- added J11: Conn_01x02_Male, Connector_PinHeader_2.54mm:PinHeader_1x02_P2.54mm_Vertical, F.Cu at (225.0, 86.1)
- added J24: Conn_02x03_Top_Bottom, KiCad:DB2ERH-2.5-2-3P-GN, F.Cu at (198.7, 75.8)
- added J53: Module conn, Connector_PinHeader_2.54mm:PinHeader_1x12_P2.54mm_Vertical, F.Cu at (193.4, 58.5)
- added K3: G2RL-1-E-DC12, Relay_THT:Relay_SPDT_Schrack-RT1-16A-FormC_RM5mm, F.Cu at (199.1, 67.3)
- added R114: 10K, Resistor_SMD:R_0603_1608Metric, F.Cu at (212.6, 77.1)
- added R115: 10K, Resistor_SMD:R_0603_1608Metric, F.Cu at (212.6, 79.7)
- added R116: 10K, Resistor_SMD:R_0603_1608Metric, F.Cu at (212.6, 82.2)
- added R117: 10K, Resistor_SMD:R_0603_1608Metric, F.Cu at (212.6, 84.7)
- added R118: 5K, Resistor_SMD:R_0603_1608Metric, F.Cu at (212.6, 87.2)
- added R119: 10K, Resistor_SMD:R_0603_1608Metric, F.Cu at (216.6, 72.1)
- added R120: 10K, Resistor_SMD:R_0603_1608Metric, F.Cu at (216.6, 74.6)
- added R121: 10K, Resistor_SMD:R_0603_1608Metric, F.Cu at (216.6, 77.1)
- added R122: 10K, Resistor_SMD:R_0603_1608Metric, F.Cu at (216.6, 79.7)
- added R123: 10K, Resistor_SMD:R_0603_1608Metric, F.Cu at (216.6, 82.2)
- added R124: 10K, Resistor_SMD:R_0603_1608Metric, F.Cu at (216.6, 84.7)
- added R125: 10K, Resistor_SMD:R_0603_1608Metric, F.Cu at (216.6, 87.2)
- added R126: 10K, Resistor_SMD:R_0603_1608Metric, F.Cu at (220.6, 72.1)
- added R127: 10K, Resistor_SMD:R_0603_1608Metric, F.Cu at (220.6, 74.6)
- added R128: 10K, Resistor_SMD:R_0603_1608Metric, F.Cu at (220.6, 77.1)
- added R129: 10K, Resistor_SMD:R_0603_1608Metric, F.Cu at (220.6, 79.7)
- added R130: 10K, Resistor_SMD:R_0603_1608Metric, F.Cu at (220.6, 82.2)
- added R131: 10K, Resistor_SMD:R_0603_1608Metric, F.Cu at (220.6, 84.7)
- added R132: 2.4K, Resistor_SMD:R_0603_1608Metric_Pad0.98x0.95mm_HandSolder, F.Cu at (228.9, 77.1)
- added R133: 2.4K, Resistor_SMD:R_0603_1608Metric_Pad0.98x0.95mm_HandSolder, F.Cu at (228.9, 79.7)
- added R134: 2.4K, Resistor_SMD:R_0603_1608Metric_Pad0.98x0.95mm_HandSolder, F.Cu at (228.9, 82.2)
- added R71: 10K, Resistor_SMD:R_0603_1608Metric, F.Cu at (208.6, 82.2)
- added R72: 10K, Resistor_SMD:R_0603_1608Metric, F.Cu at (208.6, 84.7)
- added R73: 5K, Resistor_SMD:R_0603_1608Metric, F.Cu at (208.6, 87.2)
- added R82: 10K, Resistor_SMD:R_0603_1608Metric, F.Cu at (212.6, 72.1)
- added R86: 10K, Resistor_SMD:R_0603_1608Metric, F.Cu at (212.6, 74.6)
- added U15: ADS1115IDGS, Package_SO:TSSOP-10_3x3mm_P0.5mm, F.Cu at (210.1, 90.8)
- C1: value 1uF -> 100nF; footprint Capacitor_SMD:C_0805_2012Metric -> Capacitor_SMD:C_0603_1608Metric
- C27: value 1uF -> 22nf; footprint Capacitor_SMD:C_0805_2012Metric -> Capacitor_SMD:C_0603_1608Metric_Pad1.08x0.95mm_HandSolder
- C28: value 22uF -> 1uf; footprint Capacitor_SMD:C_1206_3216Metric -> Capacitor_SMD:C_0603_1608Metric_Pad1.08x0.95mm_HandSolder
- C29: value 100nF -> 100nf; footprint Capacitor_SMD:C_0603_1608Metric -> Capacitor_SMD:C_0603_1608Metric_Pad1.08x0.95mm_HandSolder
- C30: value 4.7uF -> 1uf; footprint Capacitor_SMD:C_0805_2012Metric -> Capacitor_SMD:C_0603_1608Metric_Pad1.08x0.95mm_HandSolder
- R1, R2, R3, R4, R5, R6, R7, R8, R9: value 200R -> 1K
- R19, R20, R21, R50, R51: value 10K -> 1K
- R23, R54: value 10K -> 20R
- R24, R91: value 10K -> 1K; footprint Resistor_SMD:R_0603_1608Metric -> Resistor_SMD:R_0603_1608Metric_Pad0.98x0.95mm_HandSolder
- R25: value 10K -> 120R
- R26: value 10K -> 24K
- R27: value 10K -> 47K
- R29, R30, R31, R32, R33, R34, R35, R36, R37: value 200R -> 10K
- R38, R39, R40, R41, R42, R43, R44, R45, R46: value 1K -> 10K
- R87: value 10K -> 2K; footprint Resistor_SMD:R_0603_1608Metric -> Resistor_SMD:R_0603_1608Metric_Pad0.98x0.95mm_HandSolder
- R88, R89: value 5.1K -> 200; footprint Resistor_SMD:R_0603_1608Metric -> Resistor_SMD:R_0603_1608Metric_Pad0.98x0.95mm_HandSolder
- R90: value 4.7K -> 1K; footprint Resistor_SMD:R_0603_1608Metric -> Resistor_SMD:R_0603_1608Metric_Pad0.98x0.95mm_HandSolder
- R92: value 10K -> 2.4K; footprint Resistor_SMD:R_0603_1608Metric -> Resistor_SMD:R_0603_1608Metric_Pad0.98x0.95mm_HandSolder
- U14: value Module B1 -> NCV8114ASN150T1G; footprint Connector_PinSocket_2.54mm:PinSocket_1x12_P2.54mm_Vertical -> Package_TO_SOT_SMD:TSOT-23-5
- U17: value Module B2 -> ESP32_38p; footprint Connector_PinSocket_2.54mm:PinSocket_1x12_P2.54mm_Vertical -> KiCad:MH ET LIVE ESP-32 Dev Kit
- U23: value ESP32_38p -> XTSD04GLGEAG; footprint KiCad:MH ET LIVE ESP-32 Dev Kit -> KiCad:SON127P600X800X95-8N
- moved U17 154.8 mm to (-69.3, 165.1)
- moved U5 141.1 mm to (-69.9, 155.7)
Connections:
- net Z_Dir_THC renamed EXT_Z_Step
- net Z_Step_THC renamed EXT_Z_Dir
- C1 pad 1: +12V -> Net-(U30A-+)
- C1 pad 2: RESET -> +12V
- C26 pad 1: B_VCC -> +12V
- C27 pad 1: +12V -> Net-(U15-AIN0)
- C27 pad 2: B_RESET -> Net-(U15-AIN1)
- C28 pad 1: B_VCC -> Net-(U14-OUT)
- C28 pad 2: +12V -> Net-(D28-A)
- C29 pad 1: B_VCC -> Net-(D27-K)
- C29 pad 2: +12V -> Net-(D28-A)
- C30 pad 1: B_VCC -> Net-(J53-Pin_3)
- C30 pad 2: +12V -> Net-(J53-Pin_1)
- C4 pad 1: +3V3 -> +12V
- C5 pad 1: +3V3 -> +12V
- C6 pad 1: +3V3 -> +12V
- C7 pad 1: +3V3 -> +12V
- D10 pad 1: A_Enable_HV -> Z_Dir_HV
- D11 pad 1: A_Step_HV -> A_Enable_HV
- D12 pad 1: A_Dir_HV -> A_Step_HV
- D13 pad 1: B_Enable_HV -> A_Dir_HV
- D14 pad 1: B_Step_HV -> RLY_2_HV
- D15 pad 1: B_Dir_HV -> B_Enable_HV
- D16 pad 1: C_Enable_HV -> B_Step_HV
- D17 pad 1: C_Step_HV -> B_Dir_HV
- D18 pad 1: C_Dir_HV -> C_Enable_HV
- D7 pad 1: Z_Enable_HV -> RLY_1_HV
- D8 pad 1: Z_Step_HV -> Z_Enable_HV
- D9 pad 1: Z_Dir_HV -> Z_Step_HV
- JP1 pad 2: GPIO_0 -> GPI_0
- K1 pad A1: Net-(D26-K) -> RLY_2_HV
- K2 pad A1: Net-(D30-K) -> RLY_1_HV
- R1 pad 1: Net-(Q1-G) -> Net-(D2-A)
- R1 pad 2: X_Enable -> +12V
- R11 pad 1: Net-(D2-A) -> Net-(D11-A)
- R12 pad 1: Net-(D3-A) -> Net-(D12-A)
- R13 pad 1: Net-(D4-A) -> Net-(D13-A)
- R14 pad 1: Net-(D5-A) -> Net-(D14-A)
- R15 pad 1: Net-(D6-A) -> Net-(D15-A)
- R16 pad 1: Net-(D7-A) -> Net-(D16-A)
- R17 pad 1: Net-(D8-A) -> Net-(D17-A)
- R18 pad 1: Net-(D9-A) -> Net-(D18-A)
- R19 pad 1: +12V -> Net-(D31-A)
- R19 pad 2: Net-(Q1-G) -> +12V
- R2 pad 1: Net-(Q2-G) -> Net-(D3-A)
- R2 pad 2: X_Step -> +12V
- R20 pad 1: +12V -> Net-(D32-A)
- R20 pad 2: Net-(Q2-G) -> +12V
- R21 pad 1: +12V -> Net-(D33-A)
- R21 pad 2: Net-(Q3-G) -> +12V
- R22 pad 1: +12V -> GPI_0
- R22 pad 2: Net-(Q4-G) -> +3V3
- R23 pad 1: +12V -> Net-(D36-K)
- R23 pad 2: Net-(Q5-G) -> Net-(U29-B)
- R24 pad 1: +12V -> Net-(D27-A)
- R24 pad 2: Net-(Q6-G) -> Net-(J11-Pin_1)
- R25 pad 1: +12V -> Net-(U29-A)
- R25 pad 2: Net-(Q7-G) -> Net-(U29-B)
- R26 pad 1: +12V -> Net-(U9-VBUS)
- R26 pad 2: Net-(Q8-G) -> Net-(D19-K)
- R27 pad 2: Net-(Q9-G) -> Net-(U9-VBUS)
- R29 pad 1: Net-(Q10-G) -> +12V
- R29 pad 2: A_Enable -> RLY_1
- R3 pad 1: Net-(Q3-G) -> Net-(D4-A)
- R3 pad 2: X_Dir -> +12V
- R30 pad 1: Net-(Q11-G) -> +12V
- R30 pad 2: A_Step -> Y_Dir
- R31 pad 1: Net-(Q12-G) -> +12V
- R31 pad 2: A_Dir -> Y_Step
- R32 pad 1: Net-(Q13-G) -> +12V
- R32 pad 2: B_Enable -> Y_Enable
- R33 pad 1: Net-(Q14-G) -> +12V
- R33 pad 2: B_Step -> X_Dir
- R34 pad 1: Net-(Q15-G) -> +12V
- R34 pad 2: B_Dir -> X_Step
- R35 pad 1: Net-(Q16-G) -> +12V
- R35 pad 2: C_Enable -> X_Enable
- R36 pad 1: Net-(Q17-G) -> +12V
- R36 pad 2: C_Step -> RLY_2
- R37 pad 1: Net-(Q18-G) -> +12V
- R37 pad 2: C_Dir -> A_Dir
- R38 pad 1: Net-(D10-A) -> +12V
- R38 pad 2: +12V -> A_Step
- R39 pad 1: Net-(D11-A) -> +12V
- R39 pad 2: +12V -> A_Enable
- R4 pad 1: Net-(Q4-G) -> Net-(D5-A)
- R4 pad 2: Y_Enable -> +12V
- R40 pad 1: Net-(D12-A) -> +12V
- R40 pad 2: +12V -> Z_Dir
- R41 pad 1: Net-(D13-A) -> +12V
- R41 pad 2: +12V -> Z_Step
- R42 pad 1: Net-(D14-A) -> +12V
- R42 pad 2: +12V -> Z_Enable
- R43 pad 1: Net-(D15-A) -> +12V
- R43 pad 2: +12V -> RLY_3
- R44 pad 1: Net-(D16-A) -> +12V
- R44 pad 2: +12V -> C_Dir
- R45 pad 1: Net-(D17-A) -> +12V
- R45 pad 2: +12V -> C_Step
- R46 pad 1: Net-(D18-A) -> +12V
- R46 pad 2: +12V -> C_Enable
- R47 pad 2: Net-(Q10-G) -> B_Dir
- R48 pad 2: Net-(Q11-G) -> B_Step
- R49 pad 2: Net-(Q12-G) -> B_Enable
- R5 pad 1: Net-(Q5-G) -> Net-(D6-A)
- R5 pad 2: Y_Step -> +12V
- R50 pad 1: +12V -> Net-(D34-A)
- R50 pad 2: Net-(Q13-G) -> +3V3
- R51 pad 1: +12V -> Net-(D35-A)
- R51 pad 2: Net-(Q14-G) -> +3V3
- R52 pad 1: +12V -> Net-(U29-B)
- R52 pad 2: Net-(Q15-G) -> +3V3
- R53 pad 2: Net-(Q16-G) -> Net-(U29-A)
- R54 pad 1: +12V -> Net-(D37-K)
- R54 pad 2: Net-(Q17-G) -> Net-(U29-A)
- R55 pad 1: +12V -> RS485_TX
- R55 pad 2: Net-(Q18-G) -> +3V3
- R6 pad 1: Net-(Q6-G) -> Net-(D7-A)
- R6 pad 2: Y_Dir -> +12V
- R7 pad 1: Net-(Q7-G) -> Net-(D8-A)
- R7 pad 2: Z_Enable -> +12V
- R8 pad 1: Net-(Q8-G) -> Net-(D9-A)
- R8 pad 2: Z_Step -> +12V
- R87 pad 1: B_RESET -> Net-(J11-Pin_2)
- R87 pad 2: B_VCC -> Net-(D28-K)
- R88 pad 1: +12V -> Net-(U15-AIN0)
- R88 pad 2: B_CC1 -> Net-(D27-A)
- R89 pad 1: +12V -> Net-(U15-AIN1)
- R89 pad 2: B_CC2 -> Net-(D28-K)
- R9 pad 1: Net-(Q9-G) -> Net-(D10-A)
- R9 pad 2: Z_Dir -> +12V
- R90 pad 1: Net-(U21-~{RST}) -> Net-(U14-OUT)
- R90 pad 2: B_VCC -> Net-(U15-AIN0)
- R91 pad 1: B_RTS -> Net-(U15-AIN1)
- R91 pad 2: Net-(Q21-B) -> Net-(U14-OUT)
- R92 pad 1: B_DTR -> Net-(U15-ADDR)
- R92 pad 2: Net-(Q22-B) -> Net-(D28-A)
- U1 pad 3: I2S0_3 -> RLY_1
- U11 pad 10: unconnected-(U11-O7-Pad10) -> RLY_2_HV
- U11 pad 11: unconnected-(U11-O6-Pad11) -> A_Dir_HV
- U11 pad 12: unconnected-(U11-O5-Pad12) -> A_Step_HV
- U11 pad 13: unconnected-(U11-O4-Pad13) -> A_Enable_HV
- U11 pad 14: unconnected-(U11-O3-Pad14) -> Z_Dir_HV
- U11 pad 15: unconnected-(U11-O2-Pad15) -> Z_Step_HV
- U11 pad 16: unconnected-(U11-O1-Pad16) -> Z_Enable_HV
- U11 pad 7: I2S0_6 -> RLY_2
- U12 pad 1: MUX_SET -> EXT_MUX_EN
- U12 pad 11: Z_Step_GRBL -> Z_Dir
- U12 pad 16: B_VCC -> +12V
- U12 pad 2: Z_Enable_GRBL -> Z_Enable
- U12 pad 3: unconnected-(U12-I1a-Pad3) -> EXT_Z_Enable
- U12 pad 5: Z_Dir_GRBL -> Z_Step
- U13 pad 3: +12V -> Net-(J25-Pin_2)
- U14 pad 1: +12V -> Net-(D27-K)
- U14 pad 2: +12V -> Net-(D28-A)
- U14 pad 3: +12V -> Net-(D27-K)
- U14 pad 5: unconnected-(U14-2-Pad5) -> Net-(U14-OUT)
- U16 pad 3: +12V -> Net-(J36-Pin_2)
- U16 pad 8: A_SCLK -> Net-(J37-Pin_2)
- U16 pad 9: A_MOSI -> Net-(J38-Pin_2)
- U17 pad 1: +12V -> unconnected-(U17-SCK-Pad1)
- U17 pad 10: Net-(SW6B-B) -> RS485_EN
- U17 pad 11: Net-(SW6A-B) -> SDA
- U17 pad 12: +12V -> SCL
- U17 pad 2: +12V -> unconnected-(U17-SDO-Pad2)
- U17 pad 3: +12V -> unconnected-(U17-SDI-Pad3)
- U17 pad 4: unconnected-(U17-1-Pad4) -> CS_SD
- U17 pad 5: unconnected-(U17-2-Pad5) -> PWM1
- U17 pad 6: unconnected-(U17-3-Pad6) -> GPI_0
- U17 pad 7: unconnected-(U17-4-Pad7) -> PWM2
- U17 pad 8: B_SCLK -> RS485_RX
- U17 pad 9: B_MOSI -> RS485_TX
- U19 pad 3: +12V -> Net-(J43-Pin_2)
- U19 pad 8: A_SCLK -> Net-(J44-Pin_2)
- U19 pad 9: A_MOSI -> Net-(J45-Pin_2)
- U2 pad 3: I2S0_11 -> RLY_3
- U2 pad 6: I2S0_14 -> RLY_2
- U22 pad 3: +12V -> Net-(J48-Pin_2)
- U22 pad 8: A_SCLK -> Net-(J49-Pin_2)
- U22 pad 9: A_MOSI -> Net-(J50-Pin_2)
- U23 pad 3: unconnected-(U23-SDI-Pad3) -> SCLK
- U23 pad 4: A_CS_SD -> +12V
- U23 pad 5: A_GPIO_2 -> MOSI
- U23 pad 6: A_GPIO_0 -> CS_SD
- U23 pad 7: A_GPIO_4 -> unconnected-(U23-SD1/NC-Pad7)
- U23 pad 8: A_GPIO_16 -> +3V3
- U24 pad 10: unconnected-(U24-Pad10) -> MACRO_2
- U24 pad 11: unconnected-(U24-Pad11) -> +12V
- U24 pad 12: unconnected-(U24-Pad12) -> MACRO_1
- U24 pad 13: unconnected-(U24-Pad13) -> +12V
- U24 pad 14: unconnected-(U24-Pad14) -> RESET
- U24 pad 15: unconnected-(U24-Pad15) -> +12V
- U24 pad 16: unconnected-(U24-Pad16) -> GPI_0
- U24 pad 9: unconnected-(U24-Pad9) -> +12V
- U25 pad 10: unconnected-(U25-Pad10) -> Z_LIM
- U25 pad 11: unconnected-(U25-Pad11) -> +12V
- U25 pad 12: unconnected-(U25-Pad12) -> Y_LIM
- U25 pad 13: unconnected-(U25-Pad13) -> +12V
- U25 pad 14: unconnected-(U25-Pad14) -> X_LIM
- U25 pad 15: unconnected-(U25-Pad15) -> +12V
- U25 pad 16: unconnected-(U25-Pad16) -> MACRO_3
- U25 pad 9: unconnected-(U25-Pad9) -> +12V
- U26 pad 10: unconnected-(U26-Pad10) -> Net-(R131-Pad2)
- U26 pad 11: unconnected-(U26-Pad11) -> +12V
- U26 pad 12: unconnected-(U26-Pad12) -> C_LIM
- U26 pad 13: unconnected-(U26-Pad13) -> +12V
- U26 pad 14: unconnected-(U26-Pad14) -> B_LIM
- U26 pad 15: unconnected-(U26-Pad15) -> +12V
- U26 pad 16: unconnected-(U26-Pad16) -> A_LIM
- U26 pad 9: unconnected-(U26-Pad9) -> +12V
- U27 pad 10: unconnected-(U27-O7-Pad10) -> RLY_1_HV
- U27 pad 11: unconnected-(U27-O6-Pad11) -> Y_Dir_HV
- U27 pad 12: unconnected-(U27-O5-Pad12) -> Y_Step_HV
- U27 pad 13: unconnected-(U27-O4-Pad13) -> Y_Enable_HV
- U27 pad 14: unconnected-(U27-O3-Pad14) -> X_Dir_HV
- U27 pad 15: unconnected-(U27-O2-Pad15) -> X_Step_HV
- U27 pad 16: unconnected-(U27-O1-Pad16) -> X_Enable_HV
- U27 pad 7: I2S0_3 -> RLY_1
- U28 pad 10: unconnected-(U28-O7-Pad10) -> RLY_3_HV
- U28 pad 11: unconnected-(U28-O6-Pad11) -> C_Dir_HV
- U28 pad 12: unconnected-(U28-O5-Pad12) -> C_Step_HV
- U28 pad 13: unconnected-(U28-O4-Pad13) -> C_Enable_HV
- U28 pad 14: unconnected-(U28-O3-Pad14) -> B_Dir_HV
- U28 pad 15: unconnected-(U28-O2-Pad15) -> B_Step_HV
- U28 pad 16: unconnected-(U28-O1-Pad16) -> B_Enable_HV
- U28 pad 7: I2S0_11 -> RLY_3
- U28 pad 9: unconnected-(U28-COM-Pad9) -> +12V
- U5 pad 10: GPIO_25 -> A_LIM
- U5 pad 11: GPIO_26 -> B_LIM
- U5 pad 12: GPIO_27 -> C_LIM
- U5 pad 24: GPIO_2 -> PWM1
- U5 pad 25: GPIO_0 -> GPI_0
- U5 pad 26: GPIO_4 -> PWM2
- U5 pad 27: GPIO_16 -> RS485_RX
- U5 pad 28: I2S_WS -> RS485_TX
- U5 pad 29: GPIO_5 -> RS485_EN
- U5 pad 30: GPIO_18 -> SDA
- U5 pad 31: GPIO_19 -> SCL
- U5 pad 33: I2S_DATA -> I2S_WS
- U5 pad 34: GPIO_3 -> RXD0
- U5 pad 35: GPIO_1 -> TXD0
- U5 pad 36: I2S_BCK -> I2S_DATA
- U5 pad 37: GPIO_23 -> I2S_BCK
- U5 pad 4: GPIO_36 -> MACRO_1
- U5 pad 5: GPIO_39 -> MACRO_2
- U5 pad 6: RXD0 -> MACRO_3
- U5 pad 7: TXD0 -> X_LIM
- U5 pad 8: GPIO_32 -> Y_LIM
- U5 pad 9: GPIO_33 -> Z_LIM
- U9 pad 8: Net-(D19-K) -> Net-(U9-VBUS)
